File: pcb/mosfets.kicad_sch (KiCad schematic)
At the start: 22 parts, among them IC2 IRFR9014PBF, Q1 DMN3404L, Q2 MMBT2222A, Q3 DMN3404L, Q4 DMN3404L, Q5 DMN3404L, Q6 DMN3404L, Q7 DMN3404L

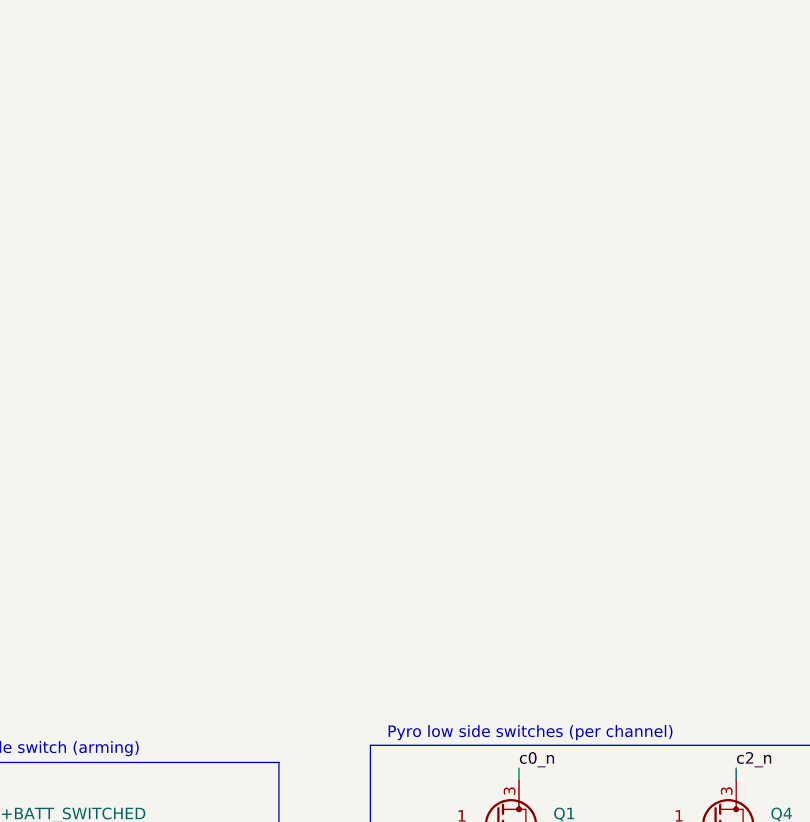
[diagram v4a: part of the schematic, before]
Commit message: added camera high side switching
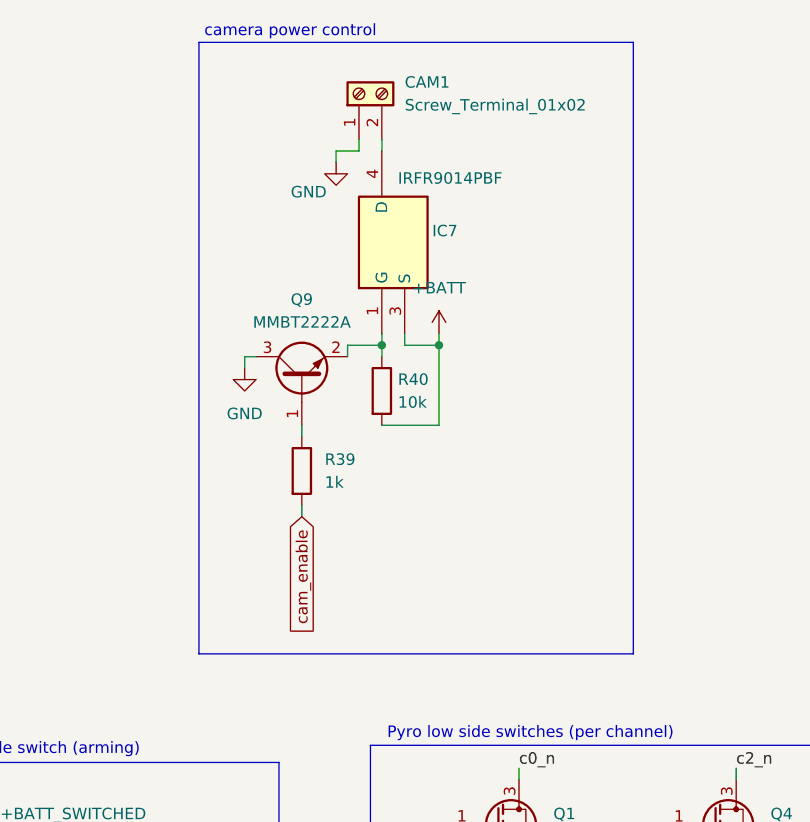
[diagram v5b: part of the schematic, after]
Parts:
- added CAM1: Screw_Terminal_01x02, footprints:TBC05021GG, symbol Connector:Screw_Terminal_01x02
- added IC7: IRFR9014PBF, footprints:TO228P990X238-3N, symbol IRFR9014PBF:IRFR9014PBF
- added Q9: MMBT2222A, Package_TO_SOT_SMD:SOT-23, symbol Transistor_BJT:MMBT2222A
- added R39: 1k, Resistor_SMD:R_0402_1005Metric, symbol Device:R
- added R40: 10k, Resistor_SMD:R_0402_1005Metric, symbol Device:R
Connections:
- net +BATT: now also IC7.3 (S), R40.2
- net GND: now also CAM1.1 (Pin_1), Q9.3 (C)
- new net: Q9.1 (B), R39.1
- new net: IC7.1 (G), Q9.2 (E), R40.1
- new net: CAM1.2 (Pin_2), IC7.4 (D)
- new net cam_enable: R39.2
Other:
- note added: "camera power control"
